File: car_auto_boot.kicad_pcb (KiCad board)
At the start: 2 copper layers, 85.1 x 63.6 mm, 15 parts, among them J1A1 Power_Terminal_1, J1B1 Power_Terminal_2, J2 Signal_Terminal, J3 Conn_01x05, SW2 SW_1, U1 ProMicro, U2 HW399_bo, U3 GY712_bo

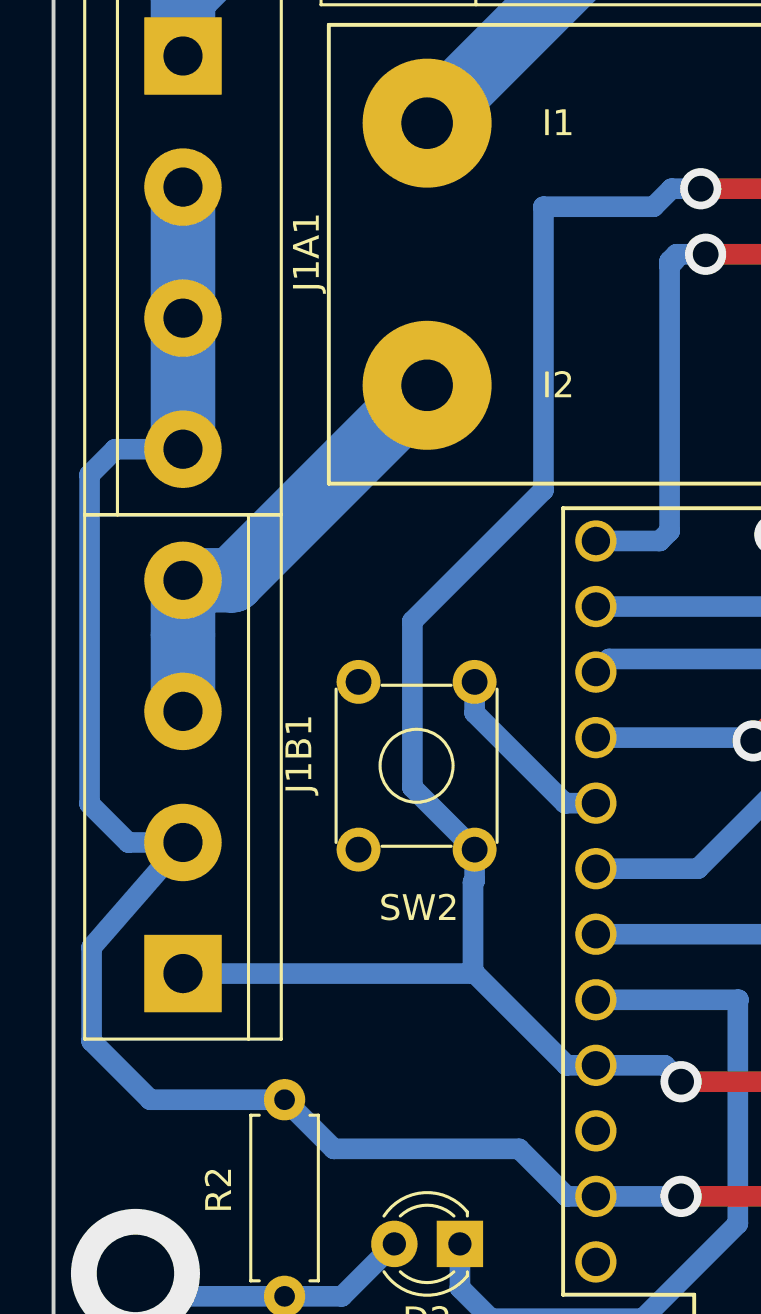
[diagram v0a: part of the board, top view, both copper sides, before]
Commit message: version with mosfet
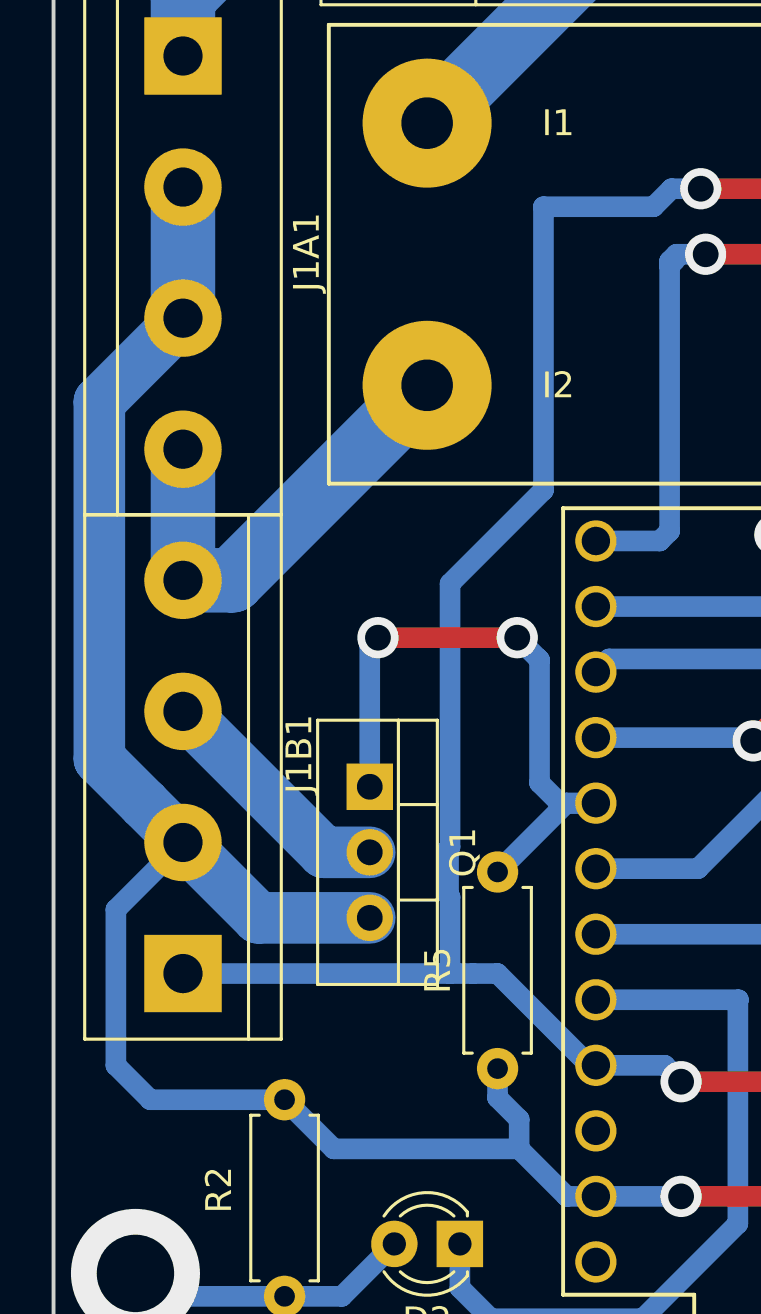
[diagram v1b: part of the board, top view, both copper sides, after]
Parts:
- removed SW2: SW_1, Buttons_Switches_THT:SW_TH_Tactile_Omron_B3F-10xx
- added Q1: IRLZ44N, TO_SOT_Packages_THT:TO-220-3_Vertical, F.Cu at (49.7, 132.9)
- added R5: 1k, Resistors_THT:R_Axial_DIN0207_L6.3mm_D2.5mm_P7.62mm_Horizontal, F.Cu at (54.7, 143.8)
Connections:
- J1A1 pad 4: -BATT -> /12V_DRIVERS
- J1B1 pad 3: /12V_DRIVERS -> /0V_DRIVERS
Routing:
- net Net-(Q1-Pad1): track 7.35 -> 24.8 mm, vias 0 -> 2
- net /0V_DRIVERS: track 0.00 -> 9.50 mm
- net -BATT: track 210.6 -> 218.8 mm
- net VCC: track 160.9 -> 160.2 mm
